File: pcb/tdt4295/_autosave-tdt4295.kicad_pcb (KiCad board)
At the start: 6 copper layers, 183 parts, among them J101 ARM 20 Pin Debug Header, J102 MCU USART1 Header, J103 DM1AA-SF-PEJ(21), J104 MCU GPIO Header, J301 FPGA__debug, J501 618015330923, J502 FPGA GPIO, P201 690-005-299-043, U101 EFM32GG12B810F1024GQ64, U102 COM-09032 Joystick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

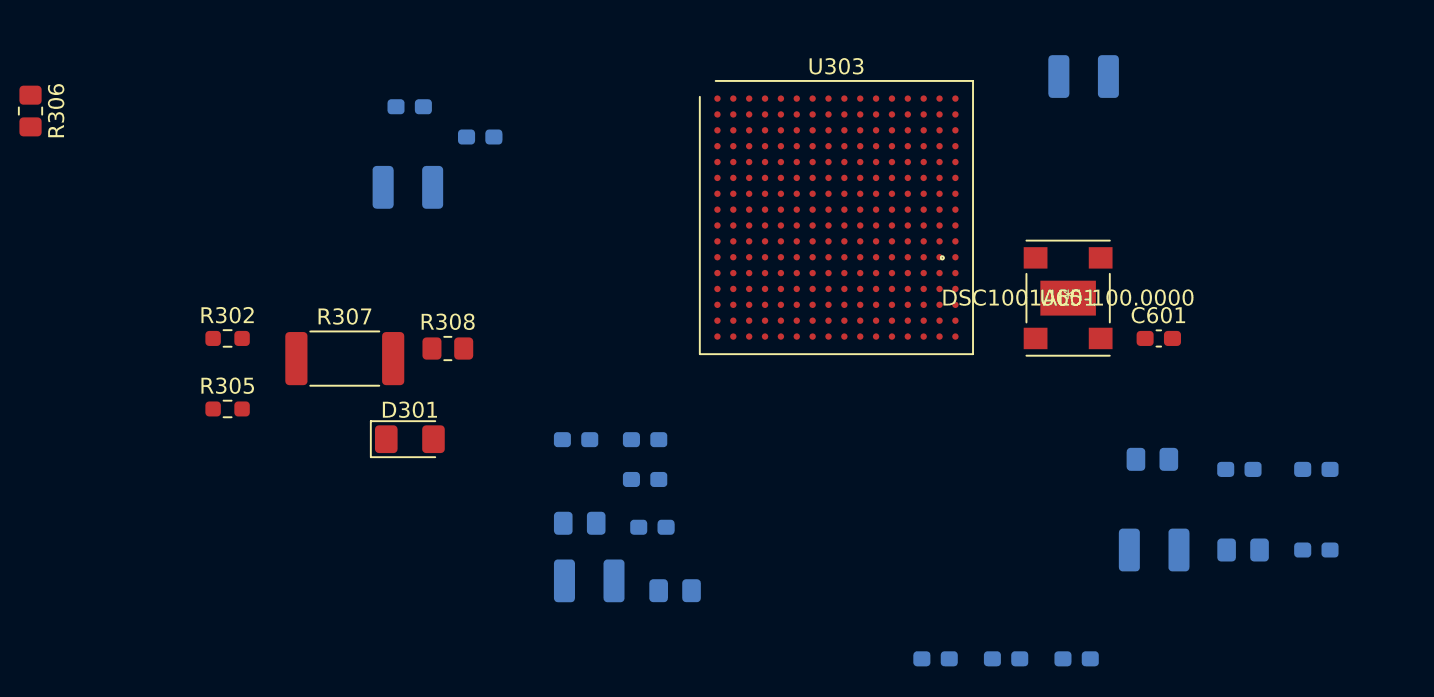
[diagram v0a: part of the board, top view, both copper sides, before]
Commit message: move capacitors to the other side, create power zones for FPGA
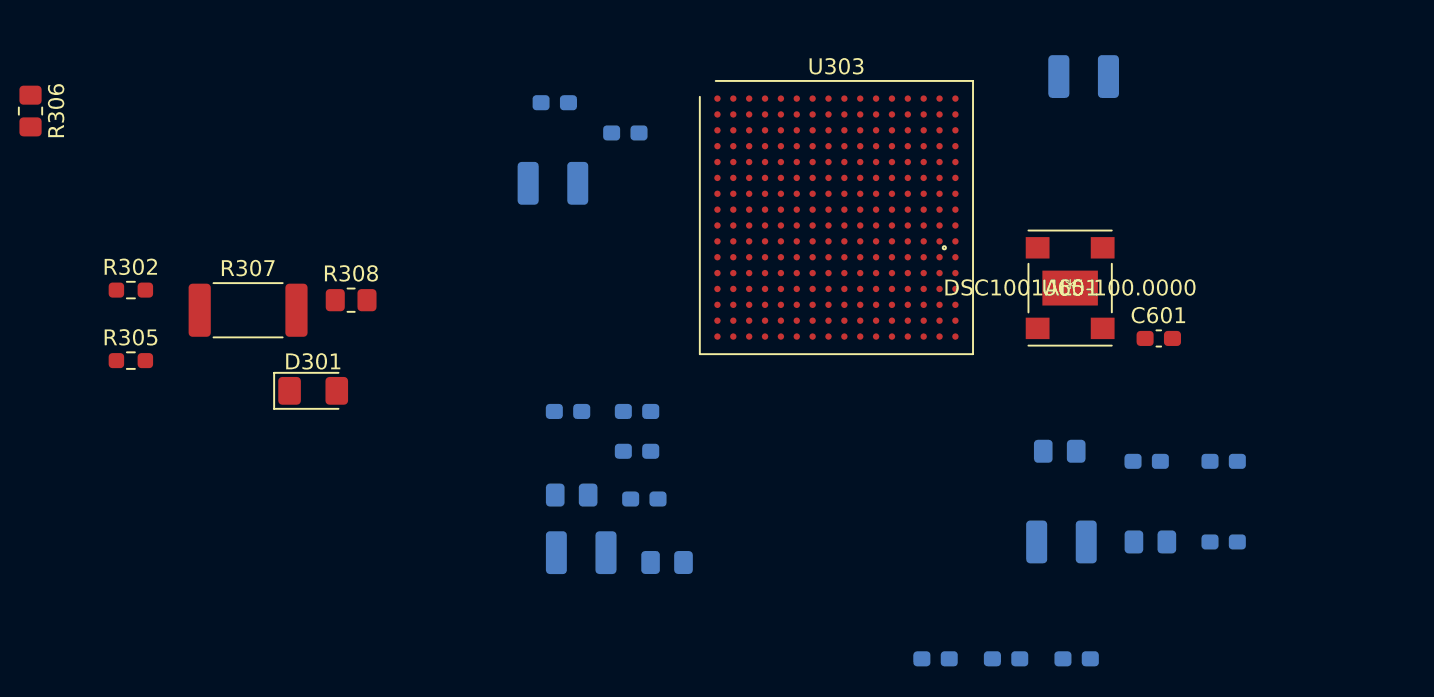
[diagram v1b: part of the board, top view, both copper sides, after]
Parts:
- moved C306 9.15 mm to (72.3, 70.9)
- moved C311 9.15 mm to (76.9, 67.7)
- moved C308 9.15 mm to (72.4, 65.8)
- moved D301 6.82 mm to (57.2, 83.9)
- moved R302 6.82 mm to (45.7, 77.6)
- moved R305 6.82 mm to (45.7, 82.0)
- moved R307 6.82 mm to (53.1, 78.9)
- moved R308 6.82 mm to (59.6, 78.2)
- moved C315 5.86 mm to (104.4, 93.5)
- moved C319 5.86 mm to (110.0, 93.5)
- moved C321 5.86 mm to (109.7, 88.4)
- moved C323 5.86 mm to (114.6, 93.5)
- moved C325 5.86 mm to (114.6, 88.4)
- moved C317 5.86 mm to (104.2, 87.8)
- moved C606 1.85 mm to (73.3, 85.2)
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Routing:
- added copper zone on 3V3, net +1V0
- added copper zone on 3V3, net +3V3
- added copper zone on 3V3, net +5V
- added copper zone on GND, net GND
- removed copper zone on In1.Cu, net +1V0
- removed copper zone on In1.Cu, net +5V
- removed copper zone on In2.Cu, net GND
